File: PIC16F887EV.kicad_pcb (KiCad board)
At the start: 2 copper layers, 5 parts, among them J2 2171750001, SW1 SW_Push, U1 PIC16F887-IP, U2 FT230XS

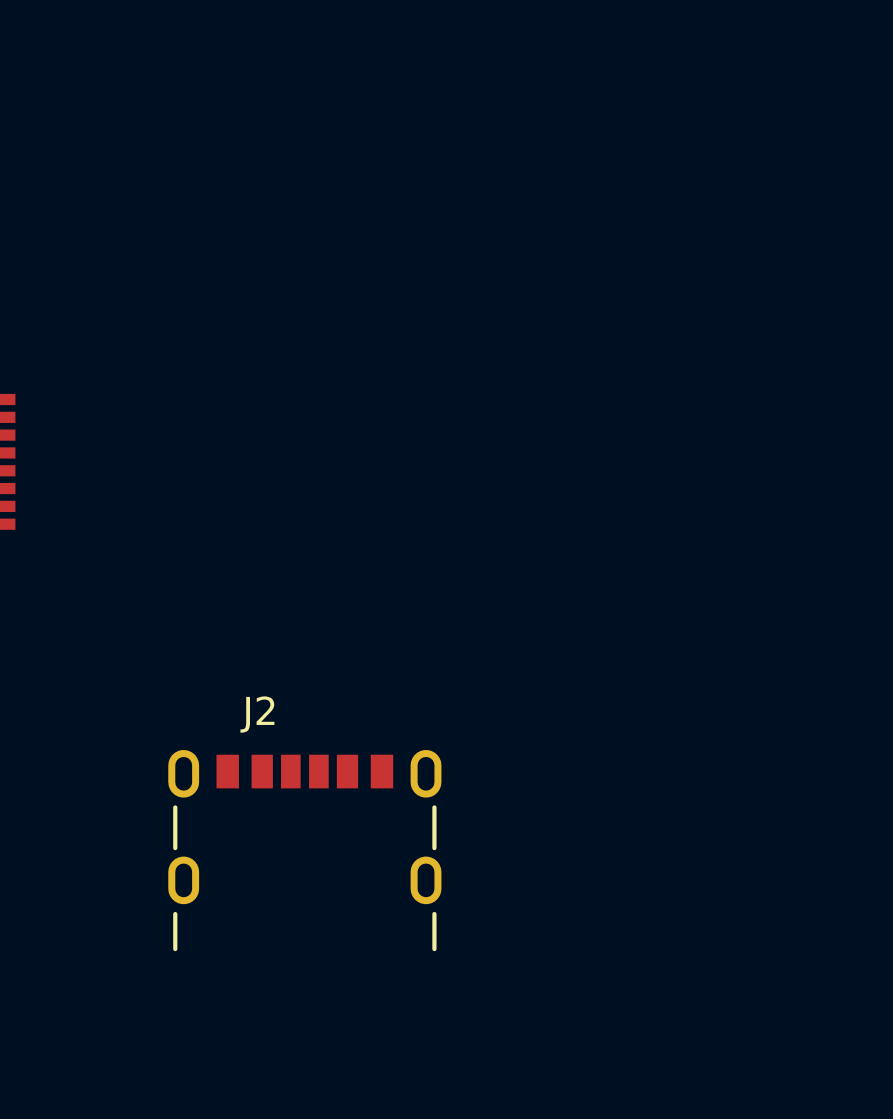
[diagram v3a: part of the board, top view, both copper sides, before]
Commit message: Puente USB completo
Agregué y conecté todos los componentes del Puente USB-USART en el esquemático
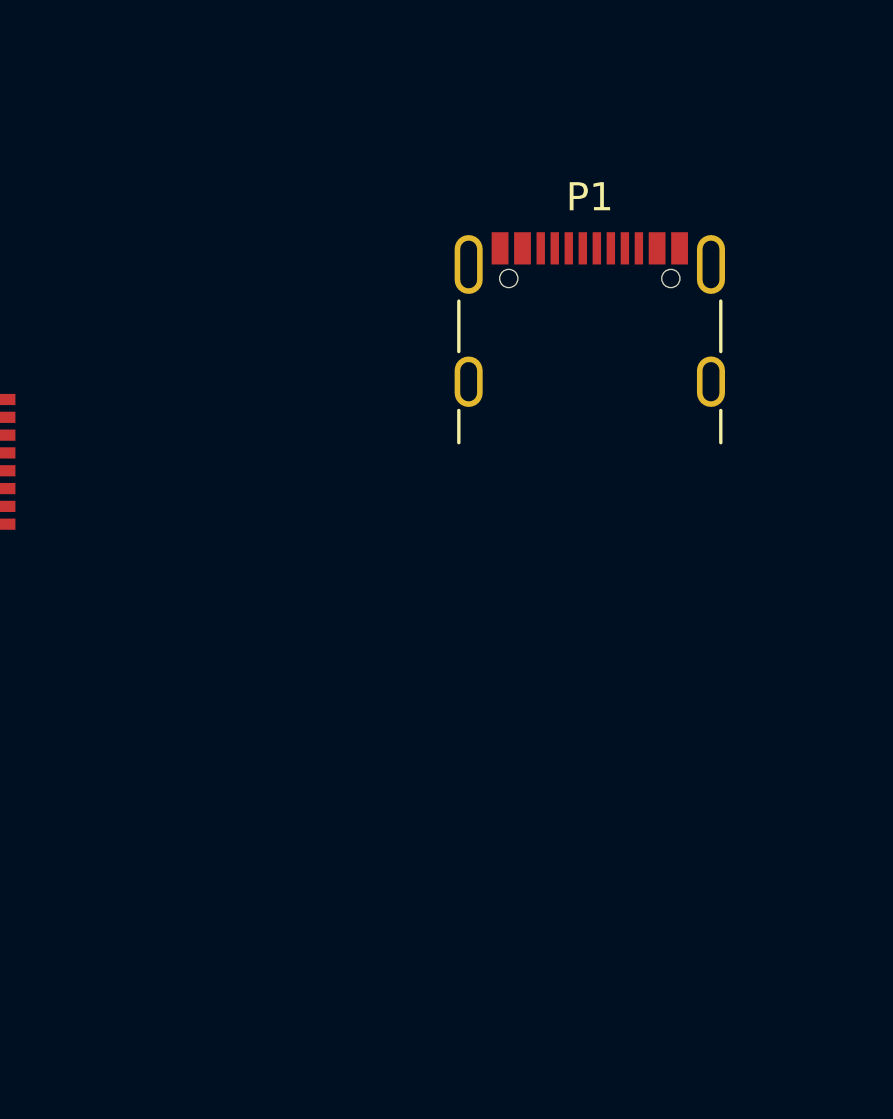
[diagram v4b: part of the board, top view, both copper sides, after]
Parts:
- removed J2: 2171750001, usbc:MOLEX_2171750001
- added P1: USB_C_Plug_USB2.0, Connector_USB:USB_C_Receptacle_GCT_USB4105-xx-A_16P_TopMnt_Horizontal, F.Cu at (196.3, 77.7)

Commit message: Actualización teclado
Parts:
- added C1: 10nF, Capacitor_SMD:C_1206_3216Metric_Pad1.33x1.80mm_HandSolder, F.Cu at (260.1, 37.8)
- added C2: 47pF, Capacitor_SMD:C_1206_3216Metric_Pad1.33x1.80mm_HandSolder, F.Cu at (260.1, 41.2)
- added C3: 47pF, Capacitor_SMD:C_1206_3216Metric_Pad1.33x1.80mm_HandSolder, F.Cu at (260.1, 44.5)
- added C4: 100nF, Capacitor_SMD:C_1206_3216Metric_Pad1.33x1.80mm_HandSolder, F.Cu at (260.1, 47.9)
- added C5: 4,7uF, Capacitor_SMD:C_1206_3216Metric_Pad1.33x1.80mm_HandSolder, F.Cu at (260.1, 51.2)
- added C6: 100nF, Capacitor_SMD:C_1206_3216Metric_Pad1.33x1.80mm_HandSolder, F.Cu at (260.1, 54.6)
- added D1: LED, LED_SMD:LED_1206_3216Metric_Pad1.42x1.75mm_HandSolder, F.Cu at (260.1, 71.1)
- added D2: LED, LED_SMD:LED_1206_3216Metric_Pad1.42x1.75mm_HandSolder, F.Cu at (260.1, 74.5)
- added FB1: FerriteBead, Inductor_SMD:L_0805_2012Metric_Pad1.15x1.40mm_HandSolder, F.Cu at (259.5, 77.7)
- added R1: 27R, Resistor_SMD:R_1206_3216Metric_Pad1.30x1.75mm_HandSolder, F.Cu at (260.1, 57.9)
- added R2: 27R, Resistor_SMD:R_1206_3216Metric_Pad1.30x1.75mm_HandSolder, F.Cu at (260.1, 61.2)
- added R3: 270R, Resistor_SMD:R_1206_3216Metric_Pad1.30x1.75mm_HandSolder, F.Cu at (260.1, 64.5)
- added R4: 270R, Resistor_SMD:R_1206_3216Metric_Pad1.30x1.75mm_HandSolder, F.Cu at (260.1, 67.8)
- added SW10: SW_Push, Button_Switch_SMD:SW_Push_1P1T_NO_6x6mm_H9.5mm, F.Cu at (240.5, 55.1)
- added SW11: SW_Push, Button_Switch_SMD:SW_Push_1P1T_NO_6x6mm_H9.5mm, F.Cu at (240.5, 62.7)
- added SW12: SW_Push, Button_Switch_SMD:SW_Push_1P1T_NO_6x6mm_H9.5mm, F.Cu at (240.5, 70.3)
- added SW13: SW_Push, Button_Switch_SMD:SW_Push_1P1T_NO_6x6mm_H9.5mm, F.Cu at (240.5, 77.9)
- added SW14: SW_Push, Button_Switch_SMD:SW_Push_1P1T_NO_6x6mm_H9.5mm, F.Cu at (251.6, 40.0)
- added SW15: SW_Push, Button_Switch_SMD:SW_Push_1P1T_NO_6x6mm_H9.5mm, F.Cu at (251.6, 47.5)
- added SW16: SW_Push, Button_Switch_SMD:SW_Push_1P1T_NO_6x6mm_H9.5mm, F.Cu at (251.6, 55.1)
- added SW2: SW_Push, Button_Switch_SMD:SW_Push_1P1T_NO_6x6mm_H9.5mm, F.Cu at (229.5, 40.0)
- added SW3: SW_Push, Button_Switch_SMD:SW_Push_1P1T_NO_6x6mm_H9.5mm, F.Cu at (229.5, 47.5)
- added SW4: SW_Push, Button_Switch_SMD:SW_Push_1P1T_NO_6x6mm_H9.5mm, F.Cu at (229.5, 55.1)
- added SW5: SW_Push, Button_Switch_SMD:SW_Push_1P1T_NO_6x6mm_H9.5mm, F.Cu at (229.5, 62.7)
- added SW6: SW_Push, Button_Switch_SMD:SW_Push_1P1T_NO_6x6mm_H9.5mm, F.Cu at (229.5, 70.3)
- added SW7: SW_Push, Button_Switch_SMD:SW_Push_1P1T_NO_6x6mm_H9.5mm, F.Cu at (229.5, 77.9)
- added SW8: SW_Push, Button_Switch_SMD:SW_Push_1P1T_NO_6x6mm_H9.5mm, F.Cu at (240.5, 40.0)
- added SW9: SW_Push, Button_Switch_SMD:SW_Push_1P1T_NO_6x6mm_H9.5mm, F.Cu at (240.5, 47.5)
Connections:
- P1 pad A1: Net-(P1-GND-PadA1) -> GND
- P1 pad A12: Net-(P1-GND-PadA1) -> GND
- P1 pad A6: unconnected-(P1-D+-PadA6) -> Net-(P1-D+)
- P1 pad A7: unconnected-(P1-D--PadA7) -> Net-(P1-D-)
- P1 pad B1: Net-(P1-GND-PadA1) -> GND
- P1 pad B12: Net-(P1-GND-PadA1) -> GND
- U1 pad 11: unconnected-(U1-VDD-Pad11) -> +5V
- U1 pad 12: unconnected-(U1-VSS-Pad12) -> GND
- U1 pad 25: unconnected-(U1-TX/CK/RC6-Pad25) -> TXpic
- U1 pad 26: unconnected-(U1-RX/DT/RC7-Pad26) -> RXpic
- U1 pad 31: unconnected-(U1-VSS-Pad31) -> GND
- U1 pad 32: unconnected-(U1-VDD-Pad32) -> +5V
- U2 pad 1: unconnected-(U2-TXD-Pad1) -> RXpic
- U2 pad 10: unconnected-(U2-3V3OUT-Pad10) -> Net-(D1-A)
- U2 pad 11: unconnected-(U2-~{RESET}-Pad11) -> Net-(D1-A)
- U2 pad 12: unconnected-(U2-VCC-Pad12) -> +5V
- U2 pad 13: unconnected-(U2-GND-Pad13) -> GND
- U2 pad 14: unconnected-(U2-CBUS1-Pad14) -> Net-(U2-CBUS1)
- U2 pad 3: unconnected-(U2-VCCIO-Pad3) -> Net-(D1-A)
- U2 pad 4: unconnected-(U2-RXD-Pad4) -> TXpic
- U2 pad 5: unconnected-(U2-GND-Pad5) -> GND
- U2 pad 7: unconnected-(U2-CBUS2-Pad7) -> Net-(U2-CBUS2)
- U2 pad 8: unconnected-(U2-USBDP-Pad8) -> Net-(U2-USBDP)
- U2 pad 9: unconnected-(U2-USBDM-Pad9) -> Net-(U2-USBDM)

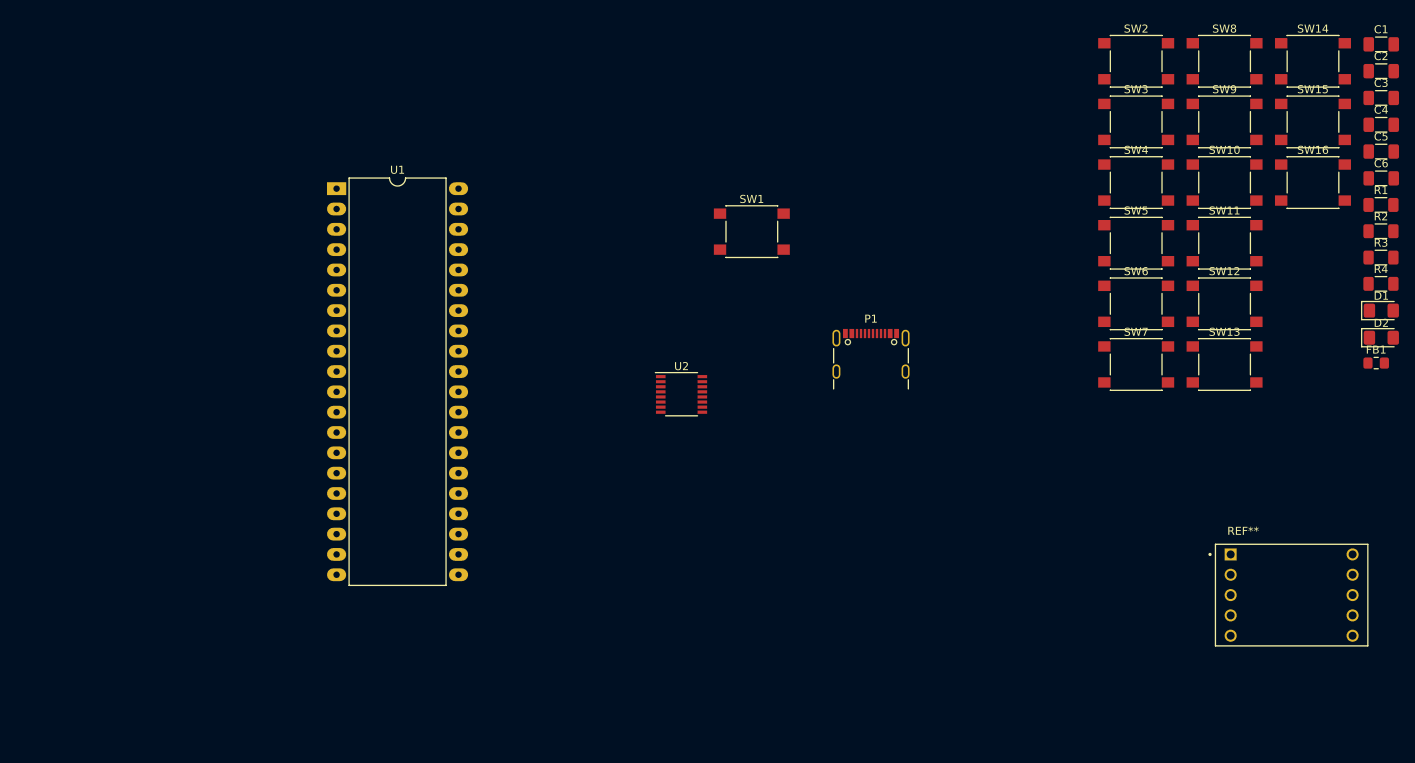
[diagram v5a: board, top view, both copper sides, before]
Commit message: Corrección leds
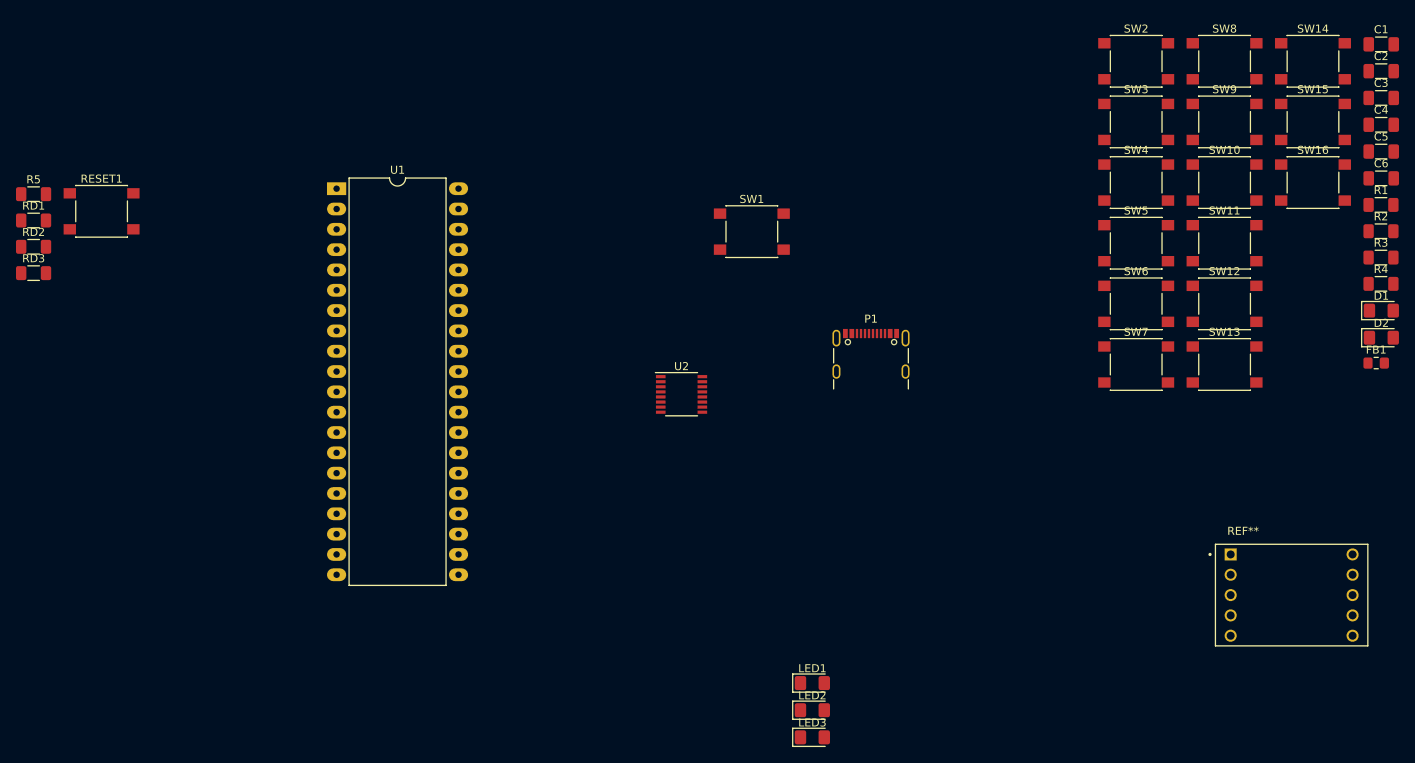
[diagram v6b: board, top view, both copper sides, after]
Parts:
- added LED1: LED, LED_SMD:LED_1206_3216Metric_Pad1.42x1.75mm_HandSolder, F.Cu at (189.0, 117.7)
- added LED2: LED, LED_SMD:LED_1206_3216Metric_Pad1.42x1.75mm_HandSolder, F.Cu at (189.0, 121.1)
- added LED3: LED, LED_SMD:LED_1206_3216Metric_Pad1.42x1.75mm_HandSolder, F.Cu at (189.0, 124.5)
- added R5: 10K, Resistor_SMD:R_1206_3216Metric_Pad1.30x1.75mm_HandSolder, F.Cu at (91.7, 56.6)
- added RD1: 220R, Resistor_SMD:R_1206_3216Metric_Pad1.30x1.75mm_HandSolder, F.Cu at (91.7, 59.9)
- added RD2: 220R, Resistor_SMD:R_1206_3216Metric_Pad1.30x1.75mm_HandSolder, F.Cu at (91.7, 63.1)
- added RD3: 220R, Resistor_SMD:R_1206_3216Metric_Pad1.30x1.75mm_HandSolder, F.Cu at (91.7, 66.4)
- added RESET1: SW_Push, Button_Switch_SMD:SW_Push_1P1T_NO_6x6mm_H9.5mm, F.Cu at (100.2, 58.7)
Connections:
- U1 pad 1: unconnected-(U1-RE3/~{MCLR}/Vpp-Pad1) -> MCLR
- U1 pad 15: unconnected-(U1-T10S0/T1CKI/RC0-Pad15) -> RC0
- U1 pad 16: unconnected-(U1-T1OSI/CCP2/RC1-Pad16) -> RC1
- U1 pad 17: unconnected-(U1-P1A/CCP1/RC2-Pad17) -> RC2
- U1 pad 2: unconnected-(U1-C12IN0-/ULPWU/AN0/RA0-Pad2) -> RA0
- U1 pad 39: unconnected-(U1-ICSPCLK/RB6-Pad39) -> ICSPCLK
- U1 pad 40: unconnected-(U1-ICSPDAT/RB7-Pad40) -> ICSPDAT

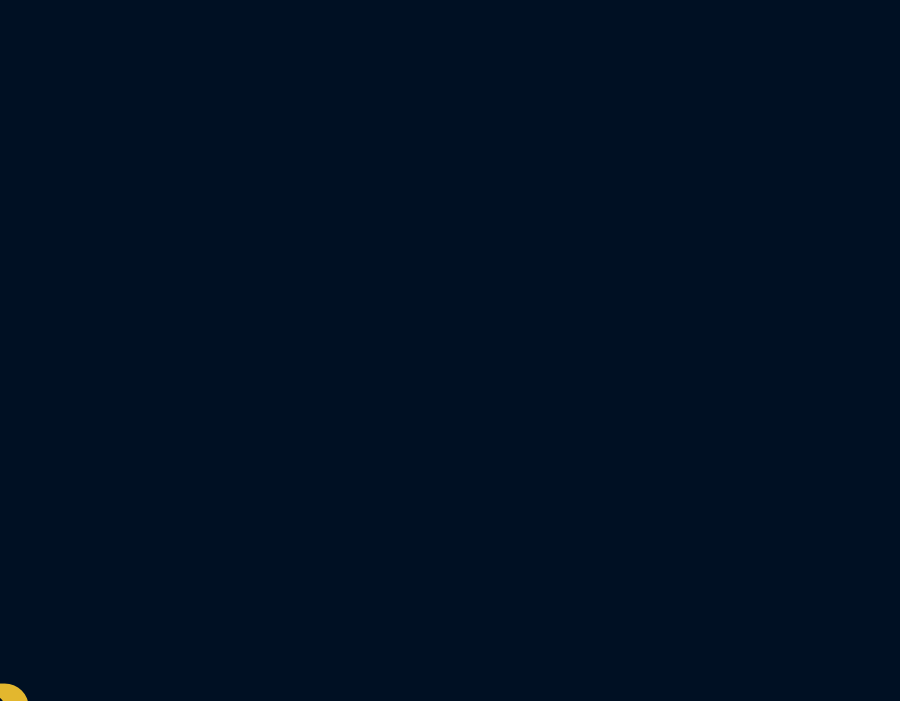
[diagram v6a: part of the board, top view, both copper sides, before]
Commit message: Socket ICSP
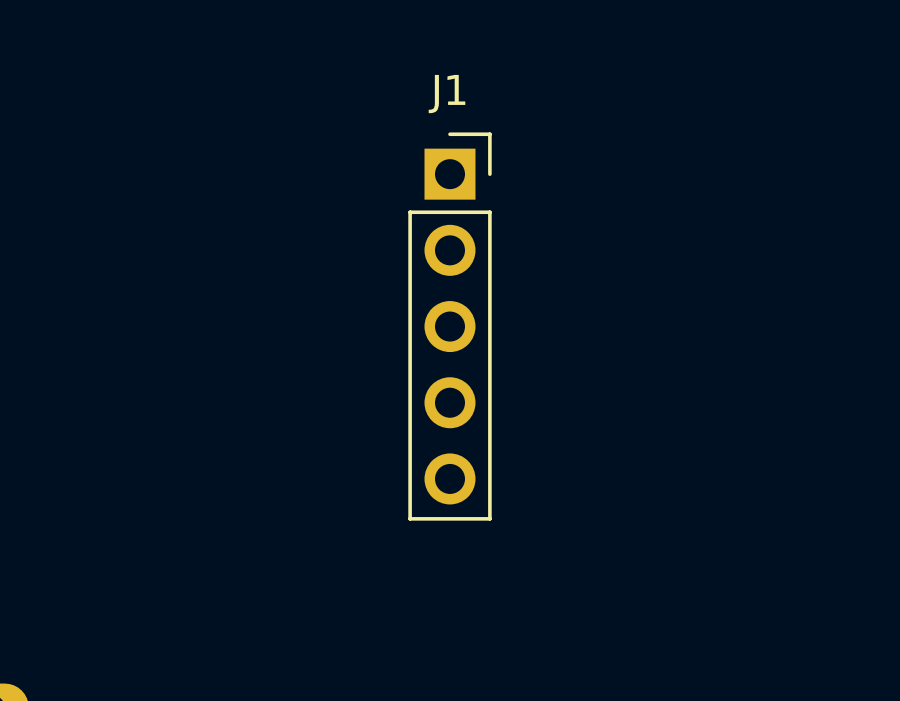
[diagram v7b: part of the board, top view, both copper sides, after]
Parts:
- added J1: Conn_01x05_Socket, Connector_PinSocket_2.54mm:PinSocket_1x05_P2.54mm_Vertical, F.Cu at (160.0, 38.1)
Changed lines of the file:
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@@
+    )
+  )
+  (footprint "Connector_PinSocket_2.54mm:PinSocket_1x05_P2.54mm_Vertical" (layer "F.Cu")
+    (at 160.02 38.1)
+    (descr "Through hole straight socket strip, 1x05, 2.54mm pitch, single row (from Kicad 4.0.7), script generated")
+    (tags "Through hole socket strip THT 1x05 2.54mm single row")
+    (property "Sheetfile" "PIC16F887EV.kicad_sch")
+    (property "Sheetname" "")
+    (property "ki_description" "Generic connector, single row, 01x05, script generated")
+    (property "ki_keywords" "connector")
+    (attr through_hole)
+    (fp_text reference "J1" (at 0 -2.77) (layer "F.SilkS")
+        (effects (font (size 1 1) (thickness 0.15)))
+    )
+    (fp_text value "Conn_01x05_Socket" (at 0 12.93) (layer "F.Fab")
+        (effects (font (size 1 1) (thickness 0.15)))
+    )
+    (fp_text user "${REFERENCE}" (at 0 5.08 90) (layer "F.Fab")
+        (effects (font (size 1 1) (thickness 0.15)))
+    )
+    (fp_line (start -1.33 1.27) (end -1.33 11.49)
+      (stroke (width 0.12) (type solid)) (layer "F.SilkS"))
+    (fp_line (start -1.33 1.27) (end 1.33 1.27)
+      (stroke (width 0.12) (type solid)) (layer "F.SilkS"))
+    (fp_line (start -1.33 11.49) (end 1.33 11.49)
+      (stroke (width 0.12) (type solid)) (layer "F.SilkS"))
+    (fp_line (start 0 -1.33) (end 1.33 -1.33)
+      (stroke (width 0.12) (type solid)) (layer "F.SilkS"))
+    (fp_line (start 1.33 -1.33) (end 1.33 0)
+      (stroke (width 0.12) (type solid)) (layer "F.SilkS"))
+    (fp_line (start 1.33 1.27) (end 1.33 11.49)
+      (stroke (width 0.12) (type solid)) (layer "F.SilkS"))
+    (fp_line (start -1.8 -1.8) (end 1.75 -1.8)
+      (stroke (width 0.05) (type solid)) (layer "F.CrtYd"))
+    (fp_line (start -1.8 11.9) (end -1.8 -1.8)
+      (stroke (width 0.05) (type solid)) (layer "F.CrtYd"))
+    (fp_line (start 1.75 -1.8) (end 1.75 11.9)
+      (stroke (width 0.05) (type solid)) (layer "F.CrtYd"))
+    (fp_line (start 1.75 11.9) (end -1.8 11.9)
+      (stroke (width 0.05) (type solid)) (layer "F.CrtYd"))
+    (fp_line (start -1.27 -1.27) (end 0.635 -1.27)
+      (stroke (width 0.1) (type solid)) (layer "F.Fab"))
+    (fp_line (start -1.27 11.43) (end -1.27 -1.27)
+      (stroke (width 0.1) (type solid)) (layer "F.Fab"))
+    (fp_line (start 0.635 -1.27) (end 1.27 -0.635)
+      (stroke (width 0.1) (type solid)) (layer "F.Fab"))
+    (fp_line (start 1.27 -0.635) (end 1.27 11.43)
+      (stroke (width 0.1) (type solid)) (layer "F.Fab"))
+    (fp_line (start 1.27 11.43) (end -1.27 11.43)
+      (stroke (width 0.1) (type solid)) (layer "F.Fab"))
+    (pad "1" thru_hole rect (at 0 0) (size 1.7 1.7) (drill 1) (layers "*.Cu" "*.Mask")
+      (net 1 "MCLR") (pinfunction "Pin_1") (pintype "passive"))
+    (pad "2" thru_hole oval (at 0 2.54) (size 1.7 1.7) (drill 1) (layers "*.Cu" "*.Mask")
+      (net 31 "+5V") (pinfunction "Pin_2") (pintype "passive"))
+    (pad "3" thru_hole oval (at 0 5.08) (size 1.7 1.7) (drill 1) (layers "*.Cu" "*.Mask")
+      (net 10 "GND") (pinfunction "Pin_3") (pintype "passive"))
+    (pad "4" thru_hole oval (at 0 7.62) (size 1.7 1.7) (drill 1) (layers "*.Cu" "*.Mask")
+      (net 62 "ICSPDAT") (pinfunction "Pin_4") (pintype "passive"))
+    (pad "5" thru_hole oval (at 0 10.16) (size 1.7 1.7) (drill 1) (layers "*.Cu" "*.Mask")
+      (net 61 "ICSPCLK") (pinfunction "Pin_5") (pintype "passive"))
+    (model "${KICAD6_3DMODEL_DIR}/Connector_PinSocket_2.54mm.3dshapes/PinSocket_1x05_P2.54mm_Vertical.wrl"
+      (offset (xyz 0 0 0))
+      (scale (xyz 1 1 1))
+      (rotate (xyz 0 0 0))
     )
   )

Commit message: Buzzer
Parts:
- removed REF**: DISPLAY_SA56-11SRWA, Downloads:DISPLAY_SA56-11SRWA
- added BZ1: Buzzer, Buzzer_Beeper:Buzzer_15x7.5RM7.6, F.Cu at (237.5, 104.1)
- added C7: 100nF, Capacitor_SMD:C_1206_3216Metric_Pad1.33x1.80mm_HandSolder, F.Cu at (221.1, 109.2)
- added R6: 330R, Resistor_SMD:R_1206_3216Metric_Pad1.30x1.75mm_HandSolder, F.Cu at (227.1, 109.2)
- added U3: MMBT2222A-7-F, Downloads:SOT103P240X110-3N, F.Cu at (100.1, 95.0)
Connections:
- U1 pad 5: unconnected-(U1-C1IN+/Vref+/AN3/RA3-Pad5) -> RA3
